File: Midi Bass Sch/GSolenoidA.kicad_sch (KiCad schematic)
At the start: 105 parts, among them Q29 BDW93C, Q30 BDW93C, Q31 BDW93C, Q32 BDW93C, Q33 BDW93C, Q34 BDW93C, Q35 BDW93C, Q36 BDW93C, Q37 BDW93C, Q38 BDW93C, Q39 BDW93C, Q40 BDW93C, Q41 BDW93C, Q42 BDW93C, Q43 BDW93C, Q44 BDW93C, Q45 BDW93C, Q46 BDW93C, Q47 BDW93C, Q48 BDW93C, U14 LTV-247, U15 LTV-247, U16 LTV-247, U17 LTV-247, U18 LTV-247

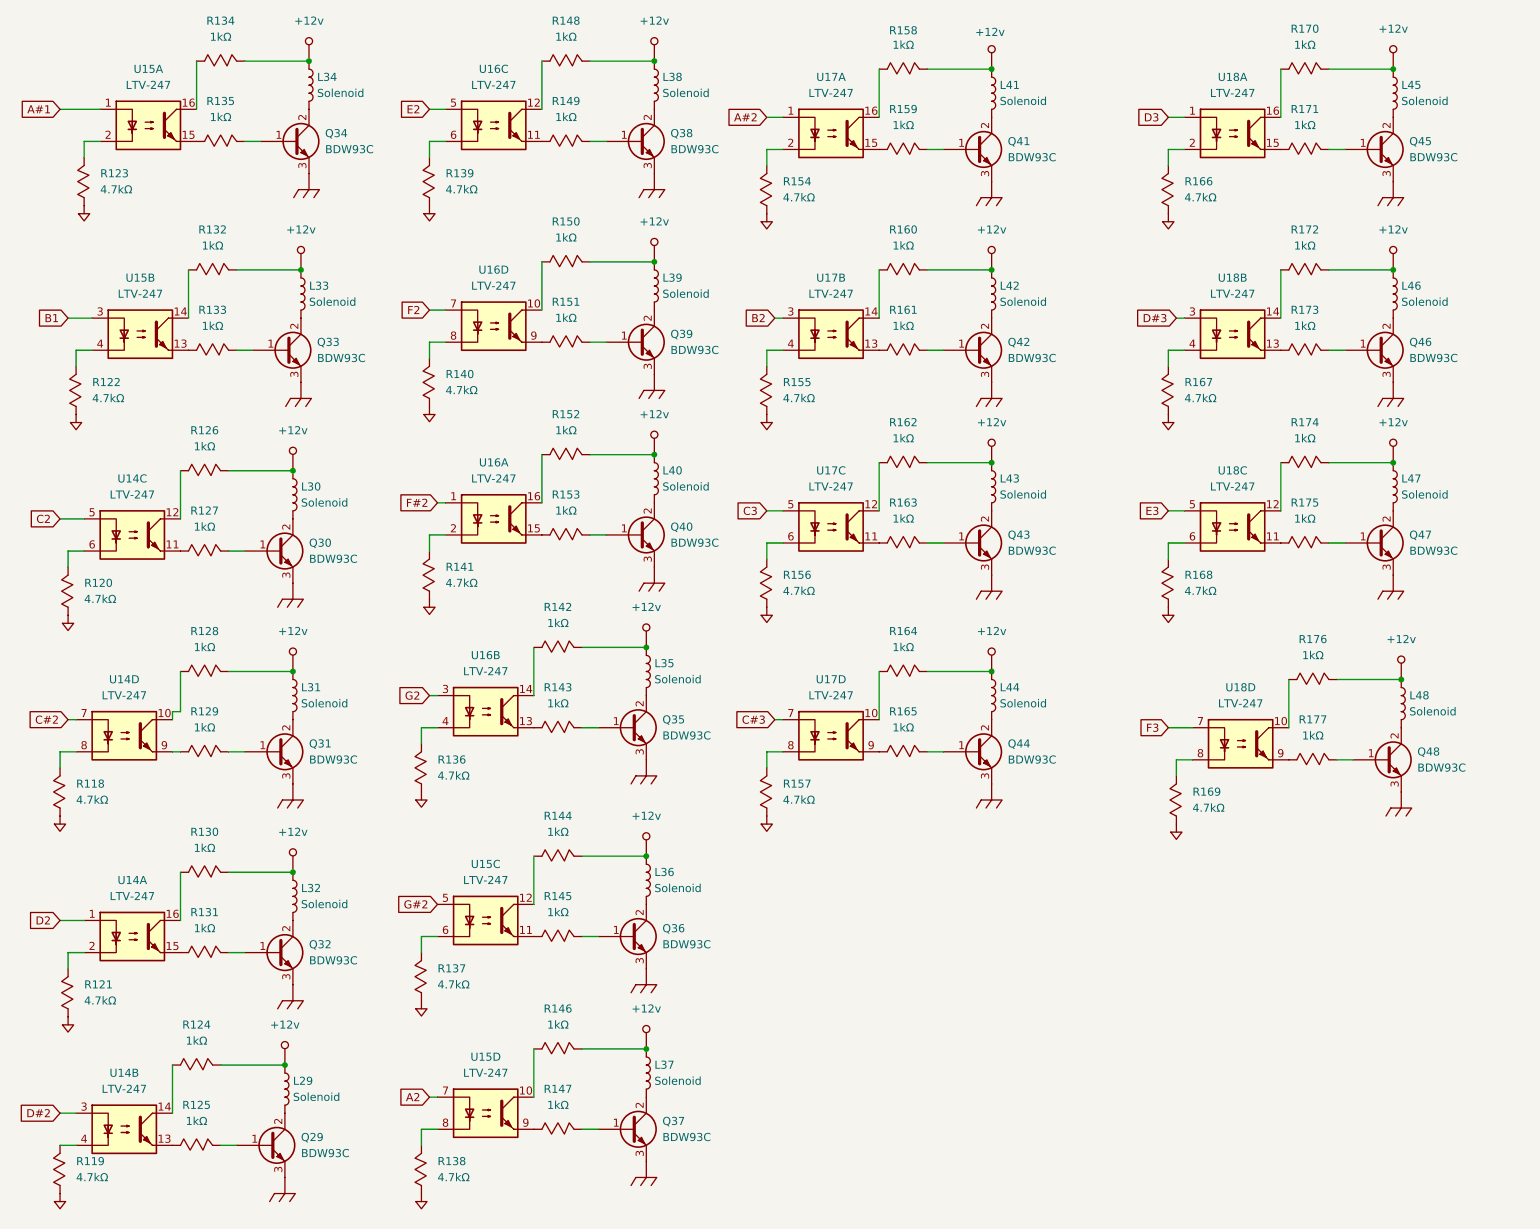
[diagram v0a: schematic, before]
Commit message: added solenoid array for the G slave
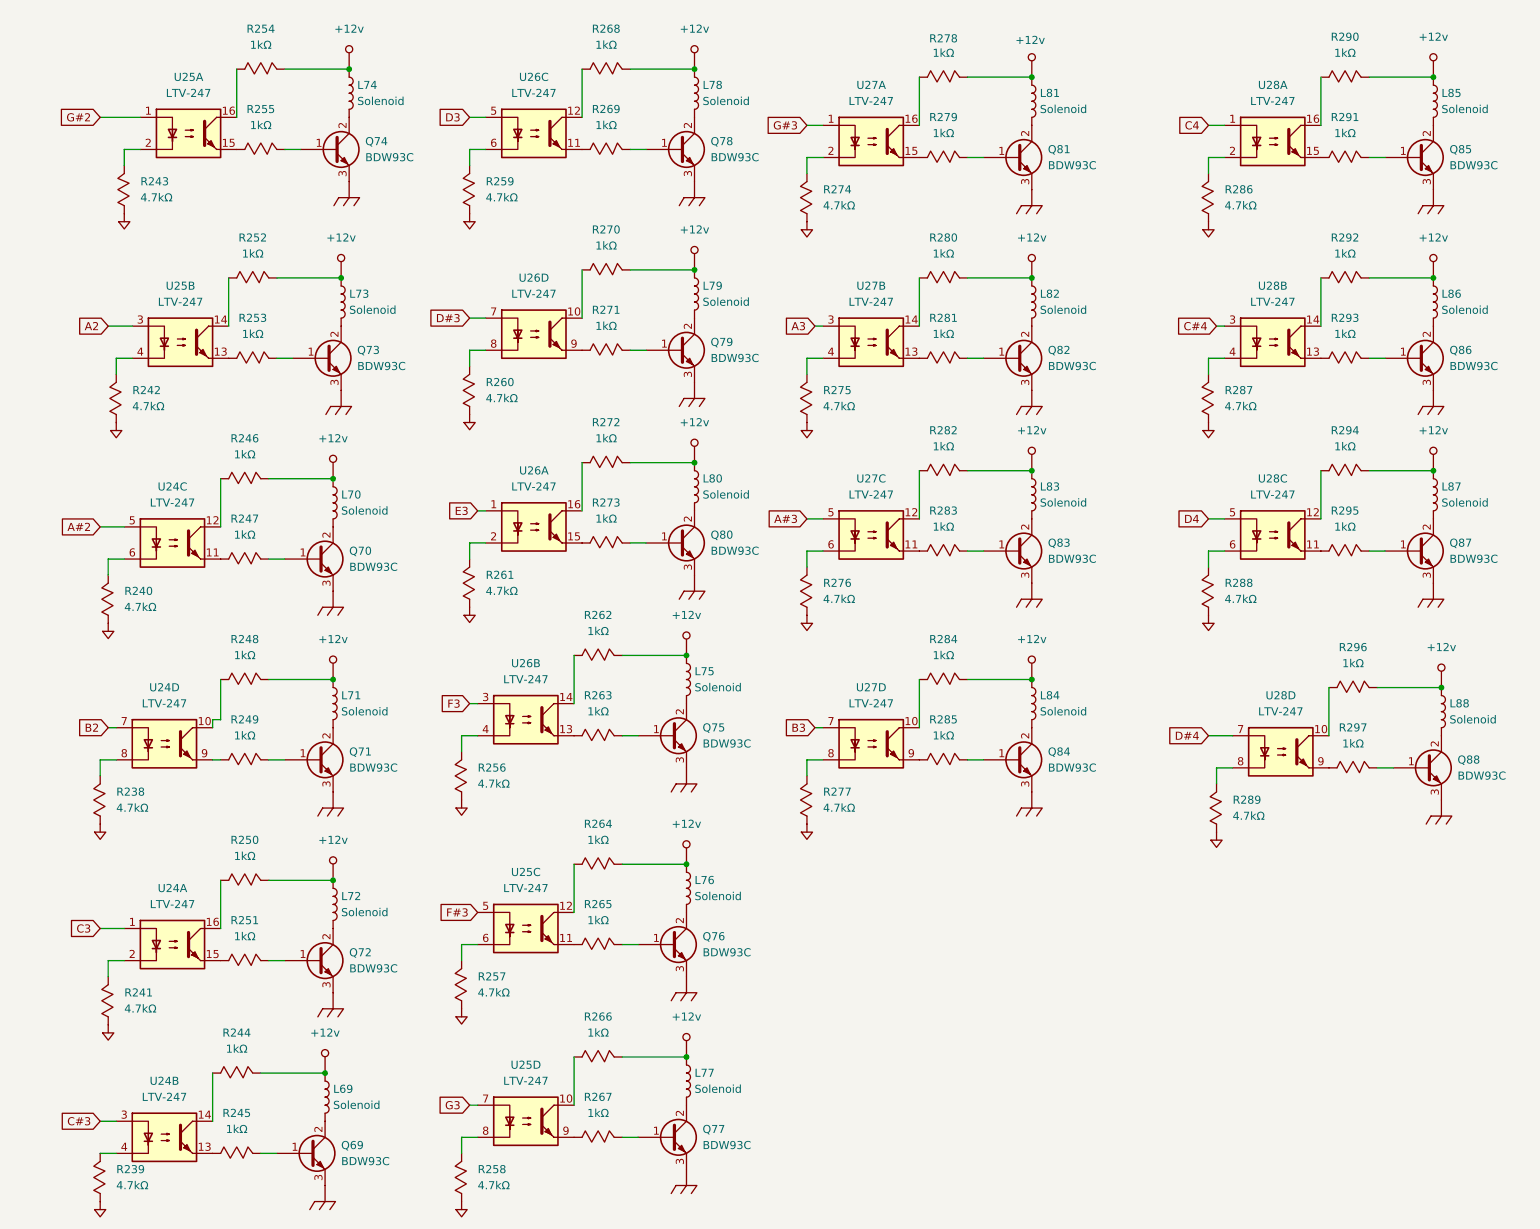
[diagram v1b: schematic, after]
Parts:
- removed L29, L30, L31, L32, L33, L34, L35, L36, L37, L38, L39, L40, L41, L42, L43, L44, L45, L46, L47, L48: Solenoid, symbol Device:L
- removed Q29, Q30, Q31, Q32, Q33, Q34, Q35, Q36, Q37, Q38, Q39, Q40, Q41, Q42, Q43, Q44, Q45, Q46, Q47, Q48: BDW93C, symbol Device:Q_NPN_BCE
- removed R118, R119, R120, R121, R122, R123, R136, R137, R138, R139, R140, R141, R154, R155, R156, R157, R166, R167, R168, R169: 4.7kΩ, symbol Owen's Symbols:Resistor_Mod
- removed R124, R125, R126, R127, R128, R129, R130, R131, R132, R133, R134, R135, R142, R143, R144, R145, R146, R147, R148, R149, R150, R151, R152, R153, R158, R159, R160, R161, R162, R163, R164, R165, R170, R171, R172, R173, R174, R175, R176, R177: 1kΩ, symbol Custom Symbols:Resistor_Mod
- removed U14, U15, U16, U17, U18: LTV-247, Package_SO:SOP-16_4.4x10.4mm_P1.27mm, symbol Isolator:LTV-247
- added L69, L70, L71, L72, L73, L74, L75, L76, L77, L78, L79, L80, L81, L82, L83, L84, L85, L86, L87, L88: Solenoid, symbol Device:L
- added Q69, Q70, Q71, Q72, Q73, Q74, Q75, Q76, Q77, Q78, Q79, Q80, Q81, Q82, Q83, Q84, Q85, Q86, Q87, Q88: BDW93C, symbol Device:Q_NPN_BCE
- added R238, R239, R240, R241, R242, R243, R256, R257, R258, R259, R260, R261, R274, R275, R276, R277, R286, R287, R288, R289: 4.7kΩ, symbol Owen's Symbols:Resistor_Mod
- added R244, R245, R246, R247, R248, R249, R250, R251, R252, R253, R254, R255, R262, R263, R264, R265, R266, R267, R268, R269, R270, R271, R272, R273, R278, R279, R280, R281, R282, R283, R284, R285, R290, R291, R292, R293, R294, R295, R296, R297: 1kΩ, symbol Custom Symbols:Resistor_Mod
- added U24, U25, U26, U27, U28: LTV-247, Package_SO:SOP-16_4.4x10.4mm_P1.27mm, symbol Isolator:LTV-247
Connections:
- net +12v: now also L69.1, L70.1, L71.1, L72.1, L73.1, L74.1, L75.1, L76.1, L77.1, L78.1, L79.1, L80.1, L81.1, L82.1, L83.1, L84.1, L85.1, L86.1, L87.1, L88.1, R244.2, R246.2, R248.2, R250.2, R252.2, R254.2, R262.2, R264.2, R266.2, R268.2, R270.2, R272.2, R278.2, R280.2, R282.2, R284.2, R290.2, R292.2, R294.2, R296.2
- net A#2: now also U24.5
- net A2: now also U25.3
- net B2: now also U24.7
- net C#3: now also U24.3
- net C3: now also U24.1
- net Chassis_GND: now also Q69.3 (E), Q70.3 (E), Q71.3 (E), Q72.3 (E), Q73.3 (E), Q74.3 (E), Q75.3 (E), Q76.3 (E), Q77.3 (E), Q78.3 (E), Q79.3 (E), Q80.3 (E), Q81.3 (E), Q82.3 (E), Q83.3 (E), Q84.3 (E), Q85.3 (E), Q86.3 (E), Q87.3 (E), Q88.3 (E)
- net D#3: now also U26.7
- net D3: now also U26.5
- net E3: now also U26.1
- net F3: now also U26.3
- net G#2: now also U25.1
- net GND: now also R238.1, R239.1, R240.1, R241.1, R242.1, R243.1, R256.1, R257.1, R258.1, R259.1, R260.1, R261.1, R274.1, R275.1, R276.1, R277.1, R286.1, R287.1, R288.1, R289.1
- new net: R239.2, U24.4
- new net: R251.1, U24.15
- new net: R250.1, U24.16
- new net: R241.2, U24.2
- new net: R259.2, U26.6
- new net: L84.2, Q84.2 (C)
- new net: L85.2, Q85.2 (C)
- new net: Q85.1 (B), R291.2
- new net: R267.1, U25.9
- new net: Q77.1 (B), R267.2
- new net: R261.2, U26.2
- new net: R262.1, U26.14
- new net: R248.1, U24.10
- new net: R238.2, U24.8
- new net: R249.1, U24.9
- new net: R290.1, U28.16
- new net: R284.1, U27.10
- new net: R277.2, U27.8
- new net: R285.1, U27.9
- new net: Q69.1 (B), R245.2
- new net: L69.2, Q69.2 (C)
- new net: R283.1, U27.11
- new net: Q83.1 (B), R283.2
- new net: Q84.1 (B), R285.2
- new net: R265.1, U25.11
- new net: R264.1, U25.12
- new net: R257.2, U25.6
- new net: R297.1, U28.9
- new net: Q88.1 (B), R297.2
- new net: Q70.1 (B), R247.2
- new net: L70.2, Q70.2 (C)
- new net: R296.1, U28.10
- new net: R255.1, U25.15
- new net: R254.1, U25.16
- new net: R243.2, U25.2
- new net: R274.2, U27.2
- new net: Q81.1 (B), R279.2
- new net: L81.2, Q81.2 (C)
- new net: R293.1, U28.13
- new net: R292.1, U28.14
- new net: R287.2, U28.4
- new net: R281.1, U27.13
- new net: R280.1, U27.14
- new net: R275.2, U27.4
- new net: R271.1, U26.9
- new net: Q79.1 (B), R271.2
- new net: Q82.1 (B), R281.2
- new net: L82.2, Q82.2 (C)
- new net: Q86.1 (B), R293.2
- new net: R279.1, U27.15
- new net: R253.1, U25.13
- new net: R252.1, U25.14
- new net: R242.2, U25.4
- new net: R266.1, U25.10
- new net: R258.2, U25.8
- new net: R270.1, U26.10
- new net: R260.2, U26.8
- new net: R291.1, U28.15
- new net: R286.2, U28.2
- new net: R276.2, U27.6
- new net: L77.2, Q77.2 (C)
- new net: R244.1, U24.14
- new net: L83.2, Q83.2 (C)
- new net: R289.2, U28.8
- new net: R272.1, U26.16
- new net: R295.1, U28.11
- new net: Q87.1 (B), R295.2
- new net: R278.1, U27.16
- new net: Q76.1 (B), R265.2
- new net: R256.2, U26.4
- new net: L87.2, Q87.2 (C)
- new net: L86.2, Q86.2 (C)
- new net: L76.2, Q76.2 (C)
- new net: R263.1, U26.13
- new net: Q75.1 (B), R263.2
- new net: Q71.1 (B), R249.2
- new net: Q72.1 (B), R251.2
- new net: L72.2, Q72.2 (C)
- new net: L75.2, Q75.2 (C)
- new net: L74.2, Q74.2 (C)
- new net: Q78.1 (B), R269.2
- new net: L78.2, Q78.2 (C)
- new net: R246.1, U24.12
- new net: L71.2, Q71.2 (C)
- new net: R245.1, U24.13
- new net: L79.2, Q79.2 (C)
- new net: R282.1, U27.12
- new net: Q74.1 (B), R255.2
- new net: Q73.1 (B), R253.2
- new net: L73.2, Q73.2 (C)
- new net: R247.1, U24.11
- new net: R240.2, U24.6
- new net: R268.1, U26.12
- new net: L88.2, Q88.2 (C)
- new net: Q80.1 (B), R273.2
- new net: L80.2, Q80.2 (C)
- new net: R294.1, U28.12
- new net: R288.2, U28.6
- new net: R273.1, U26.15
- new net: R269.1, U26.11
- new net A#3: U27.5
- new net A3: U27.3
- new net B3: U27.7
- new net C#4: U28.3
- new net C4: U28.1
- new net D#4: U28.7
- new net D4: U28.5
- new net F#3: U25.5
- new net G#3: U27.1
- new net G3: U25.7

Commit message: added footprints to kicad schematic still need footprint for din connector
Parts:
- Q69, Q70, Q71, Q72, Q73, Q74, Q75, Q76, Q77, Q78, Q79, Q80, Q81, Q82, Q83, Q84, Q85, Q86, Q87, Q88: footprint (none) -> Package_TO_SOT_THT:TO-220-3_Vertical
- R238, R239, R240, R241, R242, R243, R244, R245, R246, R247, R248, R249, R250, R251, R252, R253, R254, R255, R256, R257, R258, R259, R260, R261, R262, R263, R264, R265, R266, R267, R268, R269, R270, R271, R272, R273, R274, R275, R276, R277, R278, R279, R280, R281, R282, R283, R284, R285, R286, R287, R288, R289, R290, R291, R292, R293, R294, R295, R296, R297: footprint (none) -> Resistor_SMD:R_0805_2012Metric_Pad1.20x1.40mm_HandSolder

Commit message: working on troubleshooting section of report
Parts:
- renumbered L69 to L73, L70 to L74, L71 to L75, L72 to L76, L73 to L77, L74 to L78, L75 to L79, L76 to L80, L77 to L81, L78 to L82, L79 to L83, L80 to L84, L81 to L85, L82 to L86, L83 to L87, L84 to L88, L85 to L89, L86 to L90, L87 to L91, L88 to L92, Q69 to Q73, Q70 to Q74, Q71 to Q75, Q72 to Q76, Q73 to Q77, Q74 to Q78, Q75 to Q79, Q76 to Q80, Q77 to Q81, Q78 to Q82, Q79 to Q83, Q80 to Q84, Q81 to Q85, Q82 to Q86, Q83 to Q87, Q84 to Q88, Q85 to Q89, Q86 to Q90, Q87 to Q91, Q88 to Q92, R238 to R250, R239 to R251, R240 to R252, R241 to R253, R242 to R254, R243 to R255, R244 to R256, R245 to R257, R246 to R258, R247 to R259, R248 to R260, R249 to R261, R250 to R262, R251 to R263, R252 to R264, R253 to R265, R254 to R266, R255 to R267, R256 to R268, R257 to R269, R258 to R270, R259 to R271, R260 to R272, R261 to R273, R262 to R274, R263 to R275, R264 to R276, R265 to R277, R266 to R278, R267 to R279, R268 to R280, R269 to R281, R270 to R282, R271 to R283, R272 to R284, R273 to R285, R274 to R286, R275 to R287, R276 to R288, R277 to R289, R278 to R290, R279 to R291, R280 to R292, R281 to R293, R282 to R294, R283 to R295, R284 to R296, R285 to R297, R286 to R298, R287 to R299, R288 to R300, R289 to R301, R290 to R302, R291 to R303, R292 to R304, R293 to R305, R294 to R306, R295 to R307, R296 to R308, R297 to R309, U24 to U26, U25 to U27, U26 to U28, U27 to U29, U28 to U30
